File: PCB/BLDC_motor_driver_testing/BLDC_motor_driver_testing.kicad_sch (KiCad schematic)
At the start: 4 parts

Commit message: PCB progress...
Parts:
- added C29, C4: 100n, Capacitor_SMD:C_0504_1310Metric, symbol Device:C
- added C6, C7: 22u, symbol Device:C_Polarized
- added D3: LED, LED_SMD:LED_0402_1005Metric, symbol Device:LED
- added J2: PWR, TerminalBlock:TerminalBlock_Xinya_XY308-2.54-2P_1x02_P2.54mm_Horizontal, symbol Connector:Screw_Terminal_01x02
- added R8: 100R, Resistor_SMD:R_0402_1005Metric, symbol Device:R
- added U11: AMS1117-3.3, Package_TO_SOT_SMD:SOT-223-3_TabPin2, symbol Regulator_Linear:AMS1117-3.3
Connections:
- new net: D3.1 (K), R8.1
- new net +3.3V: C29.1, C6.1, D3.2 (A), U11.2 (VO)
- new net +5V: C4.1, C7.1, J2.2 (Pin_2), U11.3 (VI)
- new net GND: C29.2, C4.2, C6.2, C7.2, J2.1 (Pin_1), R8.2, U11.1 (GND)

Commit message: PCB progress...
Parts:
- added C3: 22u, Capacitor_SMD:C_0805_2012Metric_Pad1.18x1.45mm_HandSolder, symbol Device:C_Polarized
- added H5: 12V, MountingHole:MountingHole_2.2mm_M2_Pad_TopBottom, symbol Mechanical:MountingHole_Pad
- added H6: GND, MountingHole:MountingHole_2.2mm_M2_Pad_TopBottom, symbol Mechanical:MountingHole_Pad
- added J2: SD_IN, TerminalBlock:TerminalBlock_Xinya_XY308-2.54-3P_1x03_P2.54mm_Horizontal, symbol Connector:Screw_Terminal_01x03
- added J3: PWM_IN, TerminalBlock:TerminalBlock_Xinya_XY308-2.54-3P_1x03_P2.54mm_Horizontal, symbol Connector:Screw_Terminal_01x03
- added J4: IN_SENSE_ADC, TerminalBlock:TerminalBlock_Xinya_XY308-2.54-3P_1x03_P2.54mm_Horizontal, symbol Connector:Screw_Terminal_01x03
- C1: renamed from C4; footprint Capacitor_SMD:C_0504_1310Metric -> Capacitor_SMD:C_0805_2012Metric_Pad1.18x1.45mm_HandSolder
- C2: renamed from C7; footprint (none) -> Capacitor_SMD:C_0805_2012Metric_Pad1.18x1.45mm_HandSolder
- C4: renamed from C6; footprint (none) -> Capacitor_SMD:C_0805_2012Metric_Pad1.18x1.45mm_HandSolder
- C5: renamed from C29; footprint Capacitor_SMD:C_0504_1310Metric -> Capacitor_SMD:C_0805_2012Metric_Pad1.18x1.45mm_HandSolder
- D1: renamed from D3; footprint LED_SMD:LED_0402_1005Metric -> LED_SMD:LED_0805_2012Metric_Pad1.15x1.40mm_HandSolder
- R1: renamed from R8; footprint Resistor_SMD:R_0402_1005Metric -> Resistor_SMD:R_0805_2012Metric_Pad1.20x1.40mm_HandSolder
- renumbered J2 to J1, U11 to U1
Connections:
- net GND: now also C3.2, H6.1
- new net +12V: C3.1, H5.1
- new net IN_SENSE_A: J4.3 (Pin_3)
- new net IN_SENSE_B: J4.2 (Pin_2)
- new net IN_SENSE_C: J4.1 (Pin_1)
- new net PWM_IN_A: J3.3 (Pin_3)
- new net PWM_IN_B: J3.2 (Pin_2)
- new net PWM_IN_C: J3.1 (Pin_1)
- new net SD_A: J2.3 (Pin_3)
- new net SD_B: J2.2 (Pin_2)
- new net SD_C: J2.1 (Pin_1)
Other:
- added sheet BLDC driver phase B (driver_phaseB.kicad_sch)
- added sheet BLDC driver phase C (driver_phaseC.kicad_sch)
- sheet BLDC driver phase A: file untitled.kicad_sch -> driver_phaseA.kicad_sch
- moved on the sheet: C1, C2, C4, C5, D1, H1, H2, H3, H4, J1, R1, U1

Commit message: PCB layouting...
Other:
- sheet BLDC driver phase A ports: added GND; removed none
- sheet BLDC driver phase B ports: added GND; removed none
- sheet BLDC driver phase C ports: added GND; removed none

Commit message: Test driver layout...
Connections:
- net IN_SENSE_A: now also J4.1 (Pin_1); no longer J4.3 (Pin_3)
- net IN_SENSE_C: now also J4.3 (Pin_3); no longer J4.1 (Pin_1)
- net PWM_IN_A: now also J3.1 (Pin_1); no longer J3.3 (Pin_3)
- net PWM_IN_C: now also J3.3 (Pin_3); no longer J3.1 (Pin_1)
- net SD_A: now also J2.1 (Pin_1); no longer J2.3 (Pin_3)
- net SD_C: now also J2.3 (Pin_3); no longer J2.1 (Pin_1)

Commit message: Getting closer to finish ;)
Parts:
- J2: value SD_IN -> PHASE A
- J3: value PWM_IN -> PHASE B
- J4: value IN_SENSE_ADC -> PHASE C
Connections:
- net IN_SENSE_A is gone; now on net PWM_IN_C: J4.1 (Pin_1)
- net IN_SENSE_B is gone; now on net SD_C: J4.2 (Pin_2)
- net PWM_IN_A: now also J2.1 (Pin_1); no longer J3.1 (Pin_1)
- net PWM_IN_B: now also J3.1 (Pin_1); no longer J3.2 (Pin_2)
- net PWM_IN_C: no longer J3.3 (Pin_3)
- net SD_A: now also J2.2 (Pin_2); no longer J2.1 (Pin_1)
- net SD_B: now also J3.2 (Pin_2); no longer J2.2 (Pin_2)
- net SD_C: no longer J2.3 (Pin_3)
- net IN_SENSE_C renamed ISENSE_C
- new net ISENSE_A: J2.3 (Pin_3)
- new net ISENSE_B: J3.3 (Pin_3)

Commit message: Getting closer to finish 2 ;)
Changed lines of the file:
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@@
+	(wire
+		(pts
+			(xy 125.73 147.32) (xy 118.11 147.32)
+		)
+		(stroke
+			(width 0)
+			(type default)
+		)
+	)
 	(wire
 		(pts
@@
 	(wire
 		(pts
+			(xy 125.73 144.78) (xy 118.11 144.78)
+		)
+		(stroke
+			(width 0)
+			(type default)
+		)
+	)
+	(wire
+		(pts
 			(xy 194.31 78.74) (xy 194.31 83.82)
 		)
@@
 	(wire
 		(pts
+			(xy 125.73 124.46) (xy 118.11 124.46)
+		)
+		(stroke
+			(width 0)
+			(type default)
+		)
+	)
+	(wire
+		(pts
 			(xy 186.69 90.17) (xy 186.69 87.63)
 		)
@@
 	(wire
 		(pts
+			(xy 125.73 127) (xy 118.11 127)
+		)
+		(stroke
+			(width 0)
+			(type default)
+		)
+	)
+	(wire
+		(pts
 			(xy 156.21 101.6) (xy 142.24 101.6)
 		)
@@
 	(wire
 		(pts
+			(xy 125.73 137.16) (xy 118.11 137.16)
+		)
+		(stroke
+			(width 0)
+			(type default)
+		)
+	)
+	(wire
+		(pts
 			(xy 73.66 96.52) (xy 76.2 96.52)
 		)
@@
 	(wire
 		(pts
+			(xy 125.73 132.08) (xy 118.11 132.08)
+		)
+		(stroke
+			(width 0)
+			(type default)
+		)
+	)
+	(wire
+		(pts
 			(xy 129.54 48.26) (xy 135.89 48.26)
 		)
@@
 	(wire
 		(pts
+			(xy 125.73 134.62) (xy 118.11 134.62)
+		)
+		(stroke
+			(width 0)
+			(type default)
+		)
+	)
+	(wire
+		(pts
 			(xy 207.01 132.08) (xy 212.09 132.08)
 		)
@@
 		(pts
 			(xy 76.2 90.17) (xy 76.2 93.98)
+		)
+		(stroke
+			(width 0)
+			(type default)
+		)
+	)
+	(wire
+		(pts
+			(xy 125.73 121.92) (xy 118.11 121.92)
+		)
+		(stroke
+			(width 0)
+			(type default)
+		)
+	)
+	(wire
+		(pts
+			(xy 125.73 142.24) (xy 118.11 142.24)
 		)
 		(stroke
@@
 	(global_label "SD_B"
 		(shape input)
-		(at 118.11 134.62 0)
+		(at 125.73 134.62 0)
 		(fields_autoplaced yes)
 		(effects
@@
 		)
 		(property "Intersheetrefs" "${INTERSHEET_REFS}"
-			(at 125.8123 134.62 0)
+			(at 133.4323 134.62 0)
 			(effects
 				(font
@@
 	(global_label "SD_A"
 		(shape input)
-		(at 118.11 124.46 0)
+		(at 125.73 124.46 0)
 		(fields_autoplaced yes)
 		(effects
@@
 		)
 		(property "Intersheetrefs" "${INTERSHEET_REFS}"
-			(at 125.6309 124.46 0)
+			(at 133.2509 124.46 0)
 			(effects
 				(font
@@
 	(global_label "PWM_IN_B"
 		(shape input)
-		(at 118.11 137.16 0)
+		(at 125.73 137.16 0)
 		(fields_autoplaced yes)
 		(effects
@@
 		)
 		(property "Intersheetrefs" "${INTERSHEET_REFS}"
-			(at 130.4085 137.16 0)
+			(at 138.0285 137.16 0)
 			(effects
 				(font
@@
 	(global_label "ISENSE_B"
 		(shape input)
-		(at 118.11 132.08 0)
+		(at 125.73 132.08 0)
 		(fields_autoplaced yes)
 		(effects
@@
 		)
 		(property "Intersheetrefs" "${INTERSHEET_REFS}"
-			(at 129.9851 132.08 0)
+			(at 137.6051 132.08 0)
 			(effects
 				(font
@@
 	(global_label "PWM_IN_A"
 		(shape input)
-		(at 118.11 127 0)
+		(at 125.73 127 0)
 		(fields_autoplaced yes)
 		(effects
@@
 		)
 		(property "Intersheetrefs" "${INTERSHEET_REFS}"
-			(at 130.2271 127 0)
+			(at 137.8471 127 0)
 			(effects
 				(font
@@
 	(global_label "ISENSE_A"
 		(shape input)
-		(at 118.11 121.92 0)
+		(at 125.73 121.92 0)
 		(fields_autoplaced yes)
 		(effects
@@
 		)
 		(property "Intersheetrefs" "${INTERSHEET_REFS}"
-			(at 129.8037 121.92 0)
+			(at 137.4237 121.92 0)
 			(effects
 				(font
@@
 	(global_label "ISENSE_C"
 		(shape input)
-		(at 118.11 142.24 0)
+		(at 125.73 142.24 0)
 		(fields_autoplaced yes)
 		(effects
@@
 		)
 		(property "Intersheetrefs" "${INTERSHEET_REFS}"
-			(at 129.9851 142.24 0)
+			(at 137.6051 142.24 0)
 			(effects
 				(font
@@
 	(global_label "PWM_IN_C"
 		(shape input)
-		(at 118.11 147.32 0)
+		(at 125.73 147.32 0)
 		(fields_autoplaced yes)
 		(effects
@@
 		)
 		(property "Intersheetrefs" "${INTERSHEET_REFS}"
-			(at 130.4085 147.32 0)
+			(at 138.0285 147.32 0)
 			(effects
 				(font
@@
 	(global_label "SD_C"
 		(shape input)
-		(at 118.11 144.78 0)
+		(at 125.73 144.78 0)
 		(fields_autoplaced yes)
 		(effects
@@
 		)
 		(property "Intersheetrefs" "${INTERSHEET_REFS}"
-			(at 125.8123 144.78 0)
-			(effects
-				(font
+			(at 133.4323 144.78 0)
+			(effects
+				(font

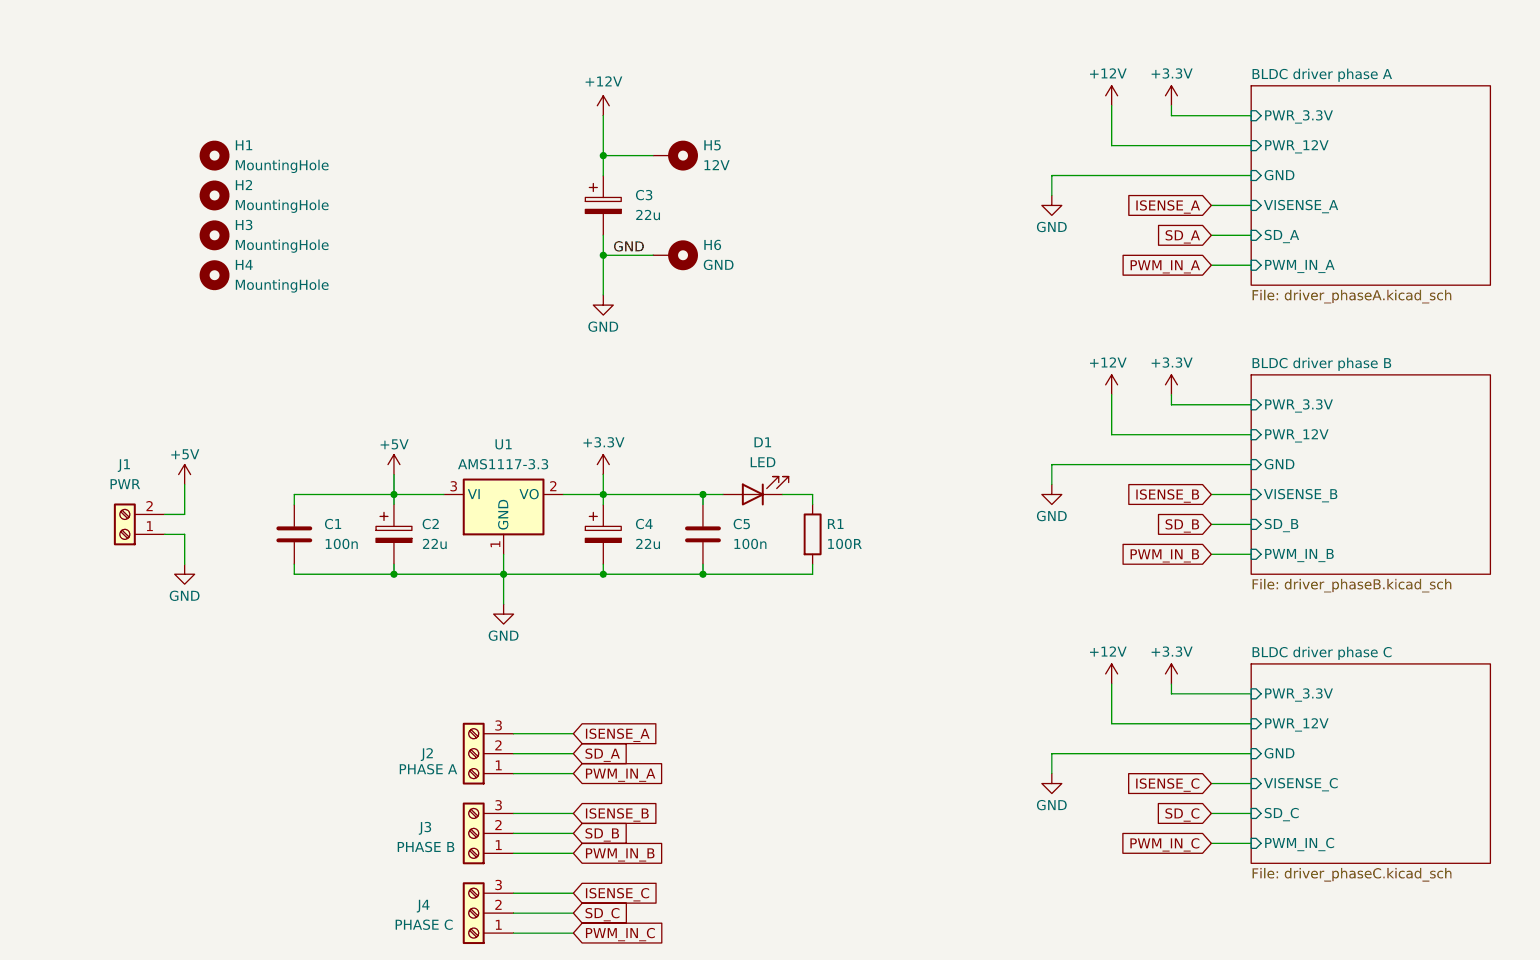
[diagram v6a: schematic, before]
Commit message: Gnd pours required, signal line EMI checking
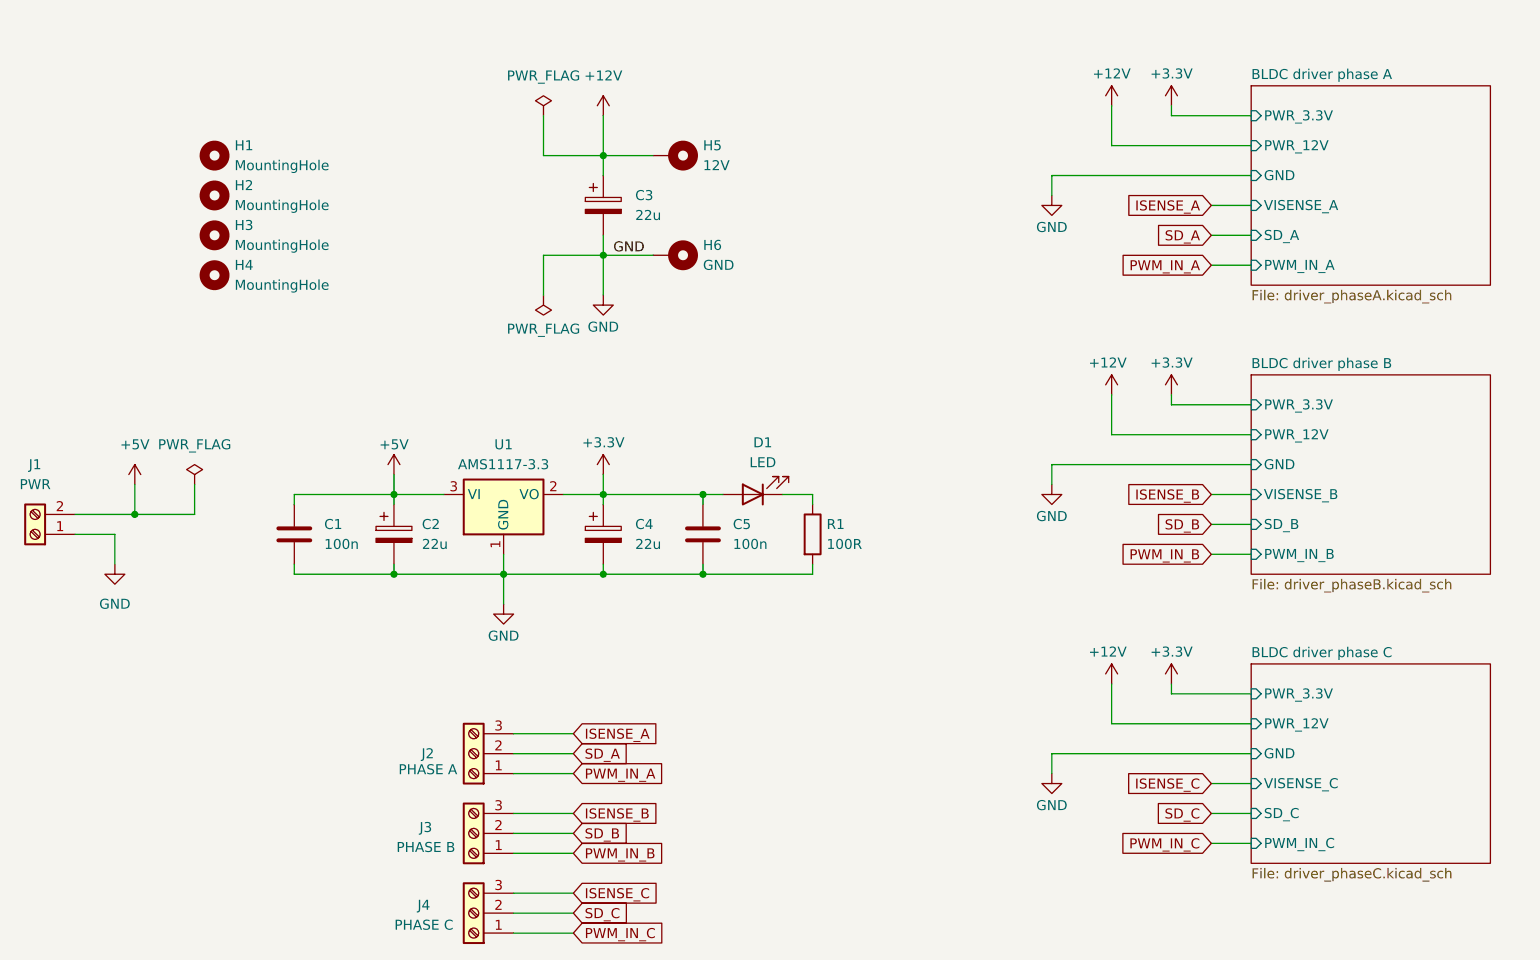
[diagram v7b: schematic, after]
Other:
- moved on the sheet: J1

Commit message: Final version of BLDC test driver
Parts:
- C3: JLCPCB Part # (none) -> C338080
- J1: JLCPCB Part # (none) -> C557685
- J2, J3, J4: JLCPCB Part # (none) -> C557686
- U1: JLCPCB Part # (none) -> C6186
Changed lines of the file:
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@@
+			)
+		)
+		(property "JLCPCB Part #" "C557686"
+			(at 113.03 134.62 0)
+			(effects
+				(font
+					(size 1.27 1.27)
+				)
+				(hide yes)
 			)
 		)
@@
 		)
 		(property "Description" "Polarized capacitor"
+			(at 129.54 54.61 0)
+			(effects
+				(font
+					(size 1.27 1.27)
+				)
+				(hide yes)
+			)
+		)
+		(property "JLCPCB Part #" "C338080"
 			(at 129.54 54.61 0)
 			(effects
@@
 		(on_board yes)
 		(dnp no)
-		(fields_autoplaced yes)
 		(property "Reference" "J1"
 			(at 57.15 87.63 0)
@@
 		(property "Description" "Generic screw terminal, single row, 01x02, script generated (kicad-library-utils/schlib/autogen/connector/)"
 			(at 57.15 96.52 0)
+			(effects
+				(font
+					(size 1.27 1.27)
+				)
+				(hide yes)
+			)
+		)
+		(property "JLCPCB Part #" "C557685"
+			(at 57.658 101.092 0)
 			(effects
 				(font
@@
 			)
 		)
+		(property "JLCPCB Part #" "C557686"
+			(at 113.03 144.78 0)
+			(effects
+				(font
+					(size 1.27 1.27)
+				)
+				(hide yes)
+			)
+		)
 		(pin "2"
 		)
@@
 			)
 		)
+		(property "JLCPCB Part #" "C6186"
+			(at 116.84 91.44 0)
+			(effects
+				(font
+					(size 1.27 1.27)
+				)
+				(hide yes)
+			)
+		)
 		(pin "2"
 		)
@@
 			(at 113.03 124.46 0)
 			(effects
+				(font
+					(size 1.27 1.27)
+				)
+				(hide yes)
+			)
+		)
+		(property "JLCPCB Part #" "C557686"
+			(at 113.03 124.46 0)
+			(effects
